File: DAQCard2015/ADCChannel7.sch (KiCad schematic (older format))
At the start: 50 parts, among them U10 LTC6403, U6 LTC6403, U7 AD9219, U8 LTC6403, U9 LTC6403

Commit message: Replaces single ample with 4-channel varients. Greatly reducing part count
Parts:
- removed C23, C33, C37, C38: .01uF, symbol C
- removed C24, C25, C29, C31, C32: .1uF, symbol C
- removed C26, C27, C28, C34, C35, C36, C39, C40, C41, C42, C43, C44: C, symbol C
- removed C30: 2.2uF, symbol CP
- removed R25, R32, R37, R38: Rt, symbol R
- removed R26, R27, R33, R34: Ri, symbol R
- removed R29, R30, R35, R36, R46: Rf, symbol R
- removed R31: 10k, symbol R
- removed R47: 2.7k, symbol R
- removed R48: 1k, symbol R
- removed U10, U6, U8, U9: LTC6403, symbol LTC6403
- removed U7: AD9219, symbol AD9219
- added C52, C53, C54: C, symbol C
- added C55: .01uF, symbol C
- added C56, C57, C58, C60, C61: .1uF, symbol C
- added C59: 2.2uF, symbol CP
- added RP16: R_PACK8, symbol R_PACK8
- added RP17, RP18: Rf, symbol R_PACK4
- added U12: THS4524IDBTR, symbol THS4524IDBTR
- added U13: AD9219, symbol AD9219
- R39, R40, R41, R42: value Ri -> Rt
- R43: value Rf -> 2.7k
- R44: value Rf -> 1k
- R45: value Rf -> 10k
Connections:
- net labels added: 3V3ana, VOCM
- net labels removed: 18ana, 3V3, Vocm
- wire segments 178 -> 192
- no-connect marks 12 -> 4
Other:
- note removed: "100R Termination \nis common for all ADCs."

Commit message: Finishes initial version of schematic(mostly). And adds a whole bunch of new footprints!
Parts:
- removed C53: C, symbol C
- removed C56, C57, C58, C60, C61: .1uF, symbol C
- removed C59: 2.2uF, symbol CP
- added C47: 10uF, extras:SMD_Cap_3mmDia, symbol CP
- added C48, C50, C51: .1uF, Capacitors_SMD:C_0603, symbol C
- added C49: .01uF, Capacitors_SMD:C_0603, symbol C
- added C53: 2.2uF, extras:SMD_Cap_3mmDia, symbol CP
- C52, C54: value C -> .1uF; footprint (none) -> Capacitors_SMD:C_0603
- C55: value .01uF -> .1uF; footprint (none) -> Capacitors_SMD:C_0603
- R39, R40, R41, R42, R43, R44, R45: footprint (none) -> Resistors_SMD:R_0603
- RP16: footprint (none) -> extras:R8_MNR18
- RP17, RP18: footprint (none) -> extras:R4-MNR04
- U12: footprint (none) -> Housings_SSOP:TSSOP-38_4.4x9.7mm_Pitch0.5mm
- U13: footprint (none) -> SMD_Packages:QFN-48-1EP
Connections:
- net 3V3ana: now also C47.1, C48.1; no longer C52.1, C54.1
- net ADC_CLK+: now also C51.2
- net ADC_CLK-: now also C50.2
- net GNDana: now also C55.1, C47.2, C48.2, C49.2; no longer C54.2, C55.2
- net VOCM: now also C49.1; no longer C55.1
- net at U13.7 (CLK-): now also C50.1
- net at U13.44 (REFT): now also C52.1, C54.2, C53.1
- net at U13.43 (REFB): now also C54.1, C55.2, C53.2
- net at U13.8 (CLK+): now also C51.1
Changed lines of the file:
@@
 $Descr A4 11693 8268
 encoding utf-8
-Sheet 3 13
+Sheet 8 13
 Title ""
 Date ""
@@
 $Comp
 L AD9219 U13
-U 1 1 55CFF5B0
+U 1 1 55CB5759
 P 9050 3700
 F 0 "U13" H 8250 4650 60  0000 C CNN
 F 1 "AD9219" H 9050 3800 60  0000 C CNN
-F 2 "" H 8650 3700 60  0000 C CNN
+F 2 "SMD_Packages:QFN-48-1EP" H 8650 3700 60  0001 C CNN
 F 3 "" H 8650 3700 60  0000 C CNN
 	1    9050 3700
@@
 $Comp
 L R R43
-U 1 1 55CFF5F3
+U 1 1 55CB5784
 P 3350 6700
 F 0 "R43" V 3430 6700 50  0000 C CNN
 F 1 "2.7k" V 3350 6700 50  0000 C CNN
-F 2 "" V 3280 6700 30  0000 C CNN
+F 2 "Resistors_SMD:R_0603" V 3280 6700 30  0001 C CNN
 F 3 "" H 3350 6700 30  0000 C CNN
 	1    3350 6700
@@
 $Comp
 L R R44
-U 1 1 55CFF5DC
+U 1 1 55CFF5DE
 P 3350 7100
 F 0 "R44" V 3430 7100 50  0000 C CNN
 F 1 "1k" V 3350 7100 50  0000 C CNN
-F 2 "" V 3280 7100 30  0000 C CNN
+F 2 "Resistors_SMD:R_0603" V 3280 7100 30  0001 C CNN
 F 3 "" H 3350 7100 30  0000 C CNN
 	1    3350 7100
@@
 Must terminate with 100R!
 $Comp
-L C C52
-U 1 1 55CFF5CD
-P 2650 6900
-F 0 "C52" H 2675 7000 50  0000 L CNN
-F 1 "C" H 2675 6800 50  0000 L CNN
-F 2 "" H 2688 6750 30  0000 C CNN
-F 3 "" H 2650 6900 60  0000 C CNN
-	1    2650 6900
-	1    0    0    -1
-$EndComp
-$Comp
-L C C53
-U 1 1 55CFF5B4
-P 2850 6900
-F 0 "C53" H 2875 7000 50  0000 L CNN
-F 1 "C" H 2875 6800 50  0000 L CNN
-F 2 "" H 2888 6750 30  0000 C CNN
-F 3 "" H 2850 6900 60  0000 C CNN
-	1    2850 6900
-	1    0    0    -1
-$EndComp
-$Comp
-L C C54
-U 1 1 55C4E847
+L C C48
+U 1 1 55CB575D
 P 3050 6900
-F 0 "C54" H 3075 7000 50  0000 L CNN
-F 1 "C" H 3075 6800 50  0000 L CNN
-F 2 "" H 3088 6750 30  0000 C CNN
+F 0 "C48" H 3075 7000 50  0000 L CNN
+F 1 ".1uF" H 3050 6800 50  0000 L CNN
+F 2 "Capacitors_SMD:C_0603" H 3088 6750 30  0001 C CNN
 F 3 "" H 3050 6900 60  0000 C CNN
 	1    3050 6900
@@
 ADC_SCLK
 $Comp
-L C C56
-U 1 1 55C50F50
+L C C50
+U 1 1 55CB5766
 P 7550 3650
-F 0 "C56" H 7575 3750 50  0000 L CNN
+F 0 "C50" H 7575 3750 50  0000 L CNN
 F 1 ".1uF" H 7575 3550 50  0000 L CNN
-F 2 "" H 7588 3500 30  0000 C CNN
+F 2 "Capacitors_SMD:C_0603" H 7588 3500 30  0001 C CNN
 F 3 "" H 7550 3650 60  0000 C CNN
 	1    7550 3650
@@
 $EndComp
 $Comp
-L C C57
-U 1 1 55CFF5E6
+L C C51
+U 1 1 55CB5745
 P 7550 3950
-F 0 "C57" H 7575 4050 50  0000 L CNN
+F 0 "C51" H 7575 4050 50  0000 L CNN
 F 1 ".1uF" H 7575 3850 50  0000 L CNN
-F 2 "" H 7588 3800 30  0000 C CNN
+F 2 "Capacitors_SMD:C_0603" H 7588 3800 30  0001 C CNN
 F 3 "" H 7550 3950 60  0000 C CNN
 	1    7550 3950
@@
 DCO+
 $Comp
-L C C61
-U 1 1 55CFF5FC
+L C C55
+U 1 1 55CB578C
 P 9300 1750
-F 0 "C61" H 9325 1850 50  0000 L CNN
+F 0 "C55" H 9325 1850 50  0000 L CNN
 F 1 ".1uF" H 9325 1650 50  0000 L CNN
-F 2 "" H 9338 1600 30  0000 C CNN
+F 2 "Capacitors_SMD:C_0603" H 9338 1600 30  0001 C CNN
 F 3 "" H 9300 1750 60  0000 C CNN
 	1    9300 1750
@@
 $EndComp
 $Comp
-L C C58
-U 1 1 55C98FC0
+L C C52
+U 1 1 55CB576C
 P 8600 1750
-F 0 "C58" H 8625 1850 50  0000 L CNN
+F 0 "C52" H 8625 1850 50  0000 L CNN
 F 1 ".1uF" H 8625 1650 50  0000 L CNN
-F 2 "" H 8638 1600 30  0000 C CNN
+F 2 "Capacitors_SMD:C_0603" H 8638 1600 30  0001 C CNN
 F 3 "" H 8600 1750 60  0000 C CNN
 	1    8600 1750
@@
 $EndComp
 $Comp
-L C C60
-U 1 1 55CFF5D7
+L C C54
+U 1 1 55CB5770
 P 8950 1650
-F 0 "C60" H 8975 1750 50  0000 L CNN
+F 0 "C54" H 8975 1750 50  0000 L CNN
 F 1 ".1uF" H 8975 1550 50  0000 L CNN
-F 2 "" H 8988 1500 30  0000 C CNN
+F 2 "Capacitors_SMD:C_0603" H 8988 1500 30  0001 C CNN
 F 3 "" H 8950 1650 60  0000 C CNN
 	1    8950 1650
@@
 GNDana
 $Comp
-L CP C59
-U 1 1 55CE4167
+L CP C53
+U 1 1 55CFF600
 P 8950 1450
-F 0 "C59" H 8975 1550 50  0000 L CNN
+F 0 "C53" H 8975 1550 50  0000 L CNN
 F 1 "2.2uF" H 8975 1350 50  0000 L CNN
-F 2 "" H 8988 1300 30  0000 C CNN
+F 2 "extras:SMD_Cap_3mmDia" H 8988 1300 30  0001 C CNN
 F 3 "" H 8950 1450 60  0000 C CNN
 	1    8950 1450
@@
 $Comp
 L R R45
-U 1 1 55CFF5EC
+U 1 1 55CB577E
 P 9900 1950
 F 0 "R45" V 9980 1950 50  0000 C CNN
 F 1 "10k" V 9900 1950 50  0000 C CNN
-F 2 "" V 9830 1950 30  0000 C CNN
+F 2 "Resistors_SMD:R_0603" V 9830 1950 30  0001 C CNN
 F 3 "" H 9900 1950 30  0000 C CNN
 	1    9900 1950
@@
 $Comp
 L THS4524IDBTR U12
-U 1 1 55CFF60B
+U 1 1 55CB579F
 P 4400 3700
 F 0 "U12" H 4700 2750 60  0000 C CNN
 F 1 "THS4524IDBTR" H 4400 4850 60  0000 C CNN
-F 2 "" H 4600 3800 60  0000 C CNN
+F 2 "Housings_SSOP:TSSOP-38_4.4x9.7mm_Pitch0.5mm" H 4600 3800 60  0001 C CNN
 F 3 "" H 4600 3800 60  0000 C CNN
 	1    4400 3700
@@
 $EndComp
 $Comp
-L C C55
-U 1 1 55CFF613
+L C C49
+U 1 1 55CB57A0
 P 3600 7100
-F 0 "C55" H 3625 7200 50  0000 L CNN
+F 0 "C49" H 3625 7200 50  0000 L CNN
 F 1 ".01uF" H 3625 7000 50  0000 L CNN
-F 2 "" H 3638 6950 30  0000 C CNN
+F 2 "Capacitors_SMD:C_0603" H 3638 6950 30  0001 C CNN
 F 3 "" H 3600 7100 60  0000 C CNN
 	1    3600 7100
@@
 Connection ~ 3600 6900
 Wire Wire Line
-	2650 6500 3750 6500
-Wire Wire Line
 	3050 6500 3050 6750
 Connection ~ 3350 6500
@@
 Connection ~ 3050 6500
 Wire Wire Line
-	2650 6500 2650 6750
-Connection ~ 2850 6500
-Wire Wire Line
-	2650 7300 3750 7300
-Wire Wire Line
 	3050 7300 3050 7050
 Wire Wire Line
 	2850 7300 2850 7050
 Connection ~ 3050 7300
-Wire Wire Line
-	2650 7300 2650 7050
-Connection ~ 2850 7300
 Wire Wire Line
 	3600 7300 3600 7250
@@
 $Comp
 L R R42
-U 1 1 55CFF617
+U 1 1 55CB57AD
 P 1850 4350
 F 0 "R42" V 1930 4350 50  0000 C CNN
 F 1 "Rt" V 1850 4350 50  0000 C CNN
-F 2 "" V 1780 4350 30  0000 C CNN
+F 2 "Resistors_SMD:R_0603" V 1780 4350 30  0001 C CNN
 F 3 "" H 1850 4350 30  0000 C CNN
 	1    1850 4350
@@
 $Comp
 L R R41
-U 1 1 55CF39BD
+U 1 1 55CB57B0
 P 1850 3850
 F 0 "R41" V 1930 3850 50  0000 C CNN
 F 1 "Rt" V 1850 3850 50  0000 C CNN
-F 2 "" V 1780 3850 30  0000 C CNN
+F 2 "Resistors_SMD:R_0603" V 1780 3850 30  0001 C CNN
 F 3 "" H 1850 3850 30  0000 C CNN
 	1    1850 3850
@@
 $Comp
 L R R40
-U 1 1 55CFF627
+U 1 1 55CB57B8
 P 1850 3350
 F 0 "R40" V 1930 3350 50  0000 C CNN
 F 1 "Rt" V 1850 3350 50  0000 C CNN
-F 2 "" V 1780 3350 30  0000 C CNN
+F 2 "Resistors_SMD:R_0603" V 1780 3350 30  0001 C CNN
 F 3 "" H 1850 3350 30  0000 C CNN
 	1    1850 3350
@@
 $Comp
 L R R39
-U 1 1 55CFF629
+U 1 1 55CB57C2
 P 1850 2850
 F 0 "R39" V 1930 2850 50  0000 C CNN
 F 1 "Rt" V 1850 2850 50  0000 C CNN
-F 2 "" V 1780 2850 30  0000 C CNN
+F 2 "Resistors_SMD:R_0603" V 1780 2850 30  0001 C CNN
 F 3 "" H 1850 2850 30  0000 C CNN
 	1    1850 2850
@@
 $Comp
 L R_PACK4 RP17
-U 1 1 55CFF630
+U 1 1 55CFF632
 P 4250 5150
 F 0 "RP17" H 4250 5600 50  0000 C CNN
 F 1 "Rf" H 4250 5100 50  0000 C CNN
-F 2 "" H 4250 5150 60  0000 C CNN
+F 2 "extras:R4-MNR04" H 4250 5150 60  0001 C CNN
 F 3 "" H 4250 5150 60  0000 C CNN
 	1    4250 5150
@@
 $Comp
 L R_PACK4 RP18
-U 1 1 55CFF639
+U 1 1 55CB574F
 P 4300 2450
 F 0 "RP18" H 4300 2900 50  0000 C CNN
 F 1 "Rf" H 4300 2400 50  0000 C CNN
-F 2 "" H 4300 2450 60  0000 C CNN
+F 2 "extras:R4-MNR04" H 4300 2450 60  0001 C CNN
 F 3 "" H 4300 2450 60  0000 C CNN
 	1    4300 2450
@@
 $Comp
 L R_PACK8 RP16
-U 1 1 55CFF63E
+U 1 1 55CB57CF
 P 2750 3600
 F 0 "RP16" H 2750 4050 50  0000 C CNN
 F 1 "R_PACK8" H 2750 3150 50  0000 C CNN
-F 2 "" H 2750 3600 60  0000 C CNN
+F 2 "extras:R8_MNR18" H 2750 3600 60  0001 C CNN
 F 3 "" H 2750 3600 60  0000 C CNN
 	1    2750 3600
@@
 Text GLabel 10150 1950 2    40   Input ~ 0
 GNDana
+Wire Wire Line
+	3750 6500 2850 6500
+Wire Wire Line
+	2850 7300 3750 7300
+$Comp
+L CP C47
+U 1 1 55CB5741
+P 2850 6900
+F 0 "C47" H 2875 7000 50  0000 L CNN
+F 1 "10uF" H 2850 6800 50  0000 L CNN
+F 2 "extras:SMD_Cap_3mmDia" H 2888 6750 30  0001 C CNN
+F 3 "" H 2850 6900 60  0000 C CNN
+	1    2850 6900
+	1    0    0    -1
+$EndComp
 $EndSCHEMATC

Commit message: Adds a more-or-less complete BOM to DAQ Card
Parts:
- C49: value .01uF -> 10000pF
- RP16: value R_PACK8 -> Ri
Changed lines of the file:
@@
 P 3600 7100
 F 0 "C49" H 3625 7200 50  0000 L CNN
-F 1 ".01uF" H 3625 7000 50  0000 L CNN
+F 1 "10000pF" H 3625 7000 50  0000 L CNN
 F 2 "Capacitors_SMD:C_0603" H 3638 6950 30  0001 C CNN
 F 3 "" H 3600 7100 60  0000 C CNN
@@
 P 2750 3600
 F 0 "RP16" H 2750 4050 50  0000 C CNN
-F 1 "R_PACK8" H 2750 3150 50  0000 C CNN
+F 1 "Ri" H 2750 3150 50  0000 C CNN
 F 2 "extras:R8_MNR18" H 2750 3600 60  0001 C CNN
 F 3 "" H 2750 3600 60  0000 C CNN

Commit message: Updates to DAQCard2015, especially to power systems
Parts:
- C47, C53: footprint extras:SMD_Cap_3mmDia -> Capacitors_SMD:C_0805
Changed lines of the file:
@@
 F 0 "C53" H 8975 1550 50  0000 L CNN
 F 1 "2.2uF" H 8975 1350 50  0000 L CNN
-F 2 "extras:SMD_Cap_3mmDia" H 8988 1300 30  0001 C CNN
+F 2 "Capacitors_SMD:C_0805" H 8988 1300 30  0001 C CNN
 F 3 "" H 8950 1450 60  0000 C CNN
 	1    8950 1450
@@
 F 0 "C47" H 2875 7000 50  0000 L CNN
 F 1 "10uF" H 2850 6800 50  0000 L CNN
-F 2 "extras:SMD_Cap_3mmDia" H 2888 6750 30  0001 C CNN
+F 2 "Capacitors_SMD:C_0805" H 2888 6750 30  0001 C CNN
 F 3 "" H 2850 6900 60  0000 C CNN
 	1    2850 6900

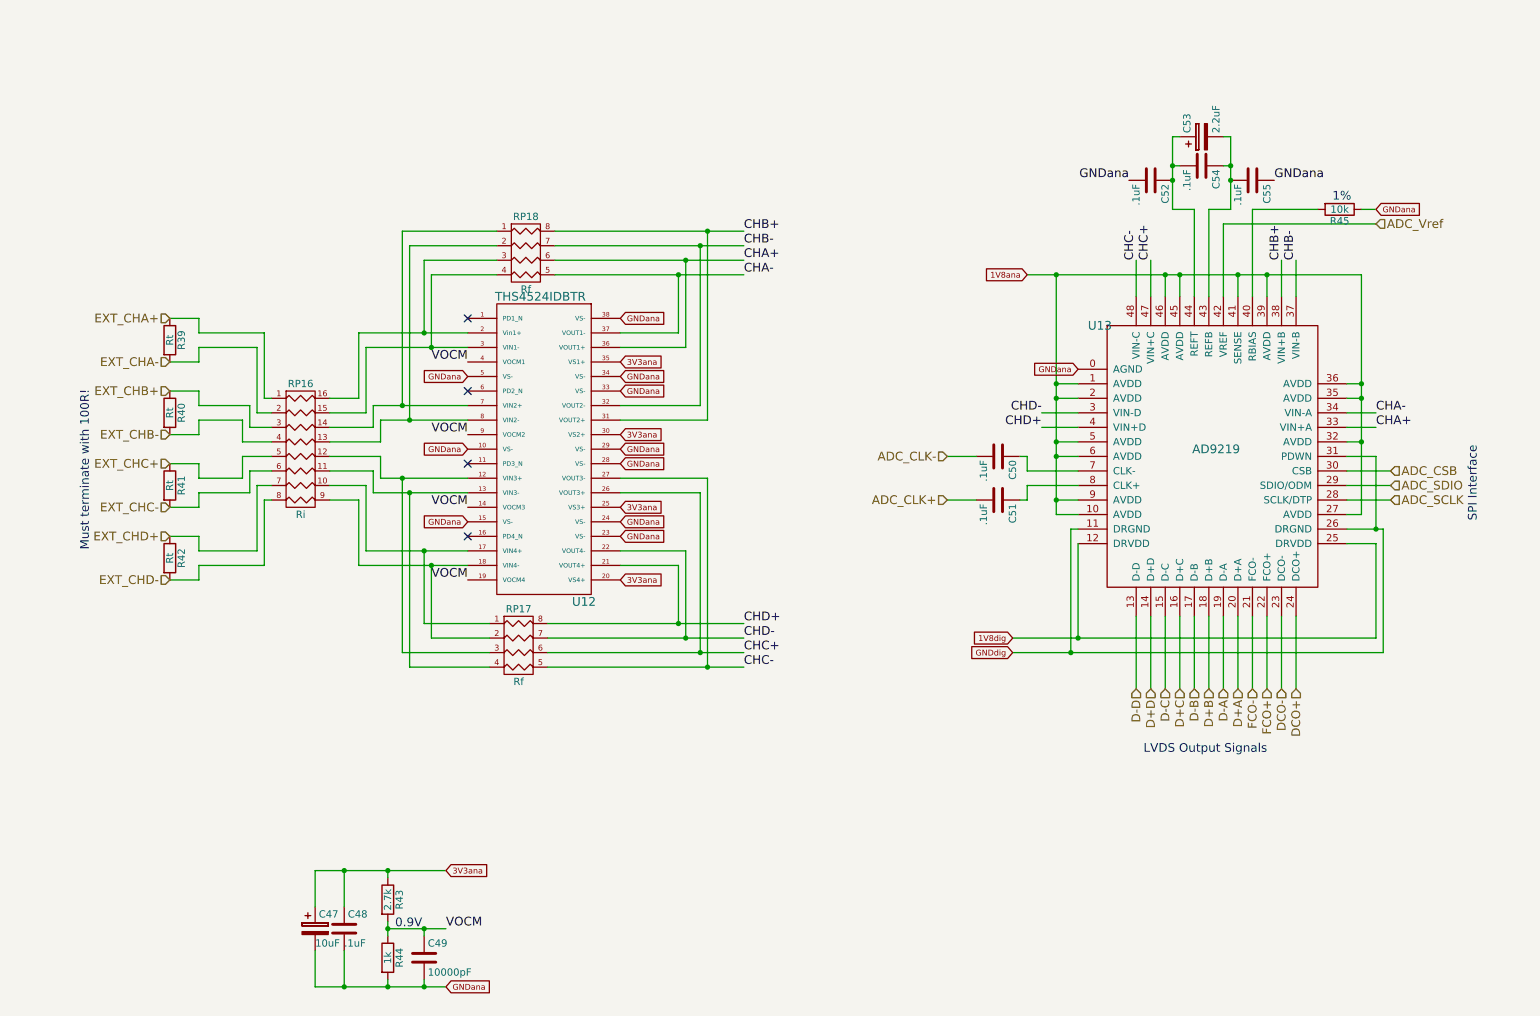
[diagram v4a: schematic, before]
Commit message: propogate previous changes to other channels and schematic
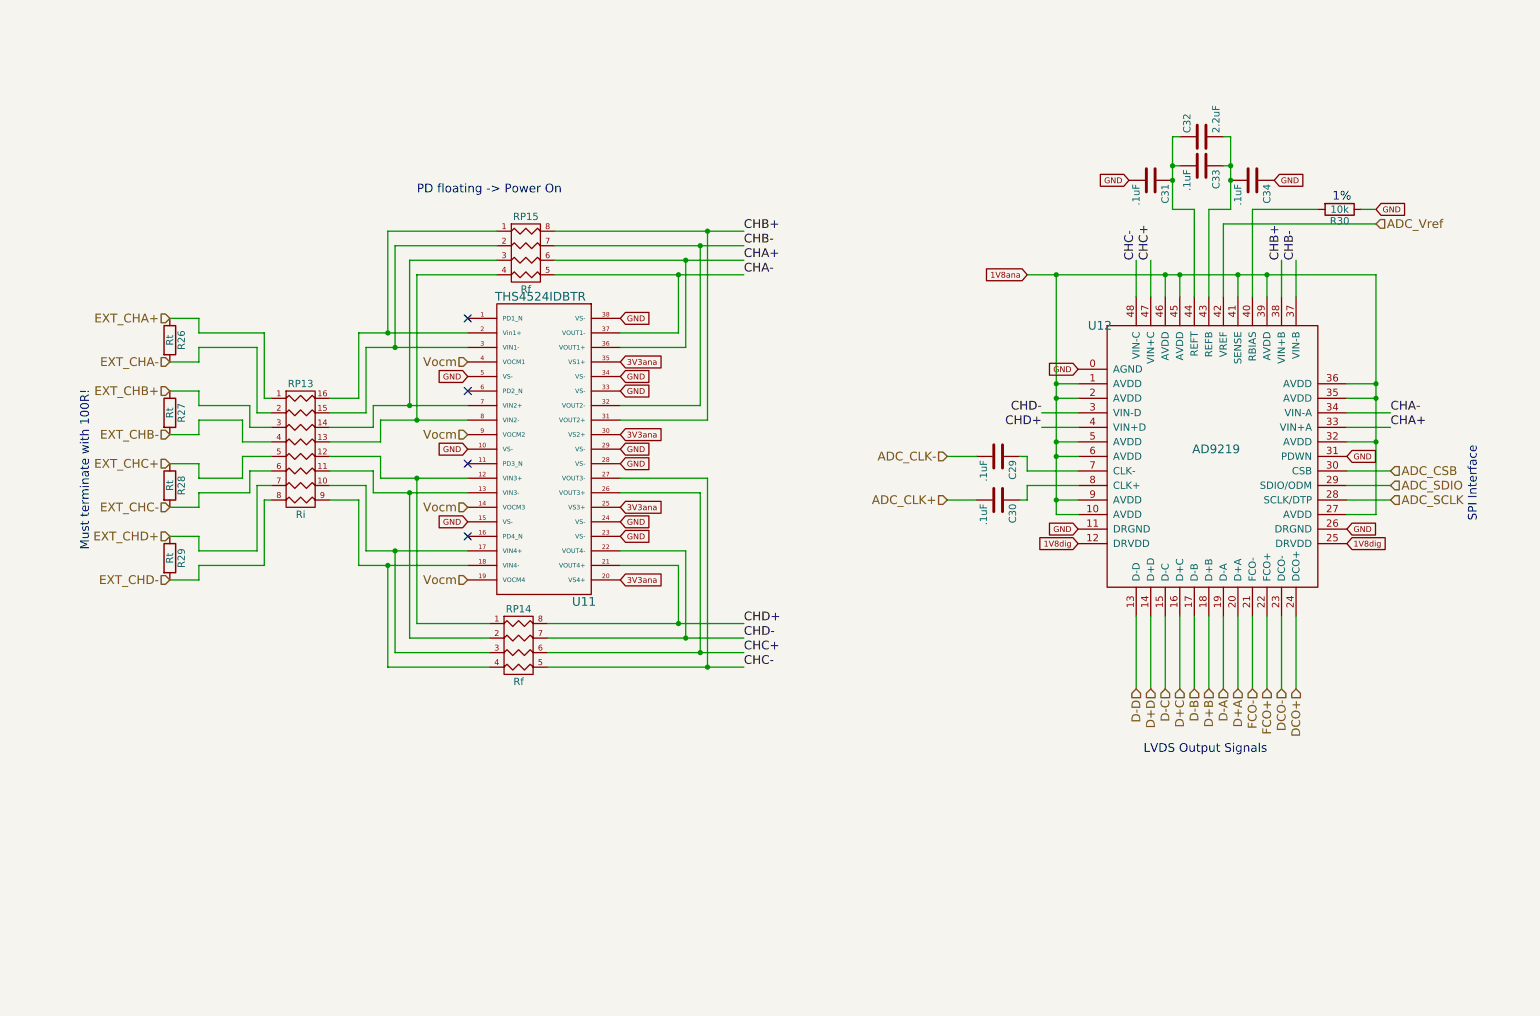
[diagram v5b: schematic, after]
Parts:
- removed C47: 10uF, Capacitors_SMD:C_0805, symbol CP
- removed C48, C50, C51, C52, C54, C55: .1uF, Capacitors_SMD:C_0603, symbol C
- removed C49: 10000pF, Capacitors_SMD:C_0603, symbol C
- removed C53: 2.2uF, Capacitors_SMD:C_0805, symbol CP
- removed R39, R40, R41, R42: Rt, Resistors_SMD:R_0603, symbol R
- removed R43: 2.7k, Resistors_SMD:R_0603, symbol R
- removed R44: 1k, Resistors_SMD:R_0603, symbol R
- removed R45: 10k, Resistors_SMD:R_0603, symbol R
- removed RP16: Ri, extras:R8_MNR18, symbol R_PACK8
- removed RP17, RP18: Rf, extras:R4-MNR04, symbol R_PACK4
- removed U12: THS4524IDBTR, Housings_SSOP:TSSOP-38_4.4x9.7mm_Pitch0.5mm, symbol THS4524IDBTR
- removed U13: AD9219, SMD_Packages:QFN-48-1EP, symbol AD9219
- added C29, C30, C31, C33, C34: .1uF, Capacitors_SMD:C_0603, symbol C
- added C32: 2.2uF, Capacitors_SMD:C_0805, symbol C
- added R26, R27, R28, R29: Rt, Resistors_SMD:R_0603, symbol R
- added R30: 10k, Resistors_SMD:R_0603, symbol R
- added RP13: Ri, extras:R8_MNR18, symbol R_PACK8
- added RP14, RP15: Rf, extras:R4-MNR04, symbol R_PACK4
- added U11: THS4524IDBTR, Housings_SSOP:TSSOP-38_4.4x9.7mm_Pitch0.5mm, symbol THS4524IDBTR
- added U12: AD9219, extras:QFN-48-1EP, symbol AD9219
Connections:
- net 1V8ana: now also U12.1 (AVDD), U12.10 (AVDD), U12.2 (AVDD), U12.27 (AVDD), U12.32 (AVDD), U12.35 (AVDD), U12.36 (AVDD), U12.39 (AVDD), U12.41 (SENSE), U12.45 (AVDD), U12.46 (AVDD), U12.5 (AVDD), U12.6 (AVDD), U12.9 (AVDD)
- net 1V8dig: now also U12.12 (DRVDD), U12.25 (DRVDD)
- net 3V3ana: now also U11.20 (VS4+), U11.25 (VS3+), U11.30 (VS2+), U11.35 (VS1+)
- net ADC_CLK+: now also C30.2
- net ADC_CLK-: now also C29.2
- net ADC_CSB: now also U12.30 (CSB)
- net ADC_SCLK: now also U12.28 (SCLK/DTP)
- net ADC_SDIO: now also U12.29 (SDIO/ODM)
- net ADC_Vref: now also U12.42 (VREF)
- net CHA+: now also RP15.6 (R3), U11.36 (VOUT1+), U12.33 (VIN+A)
- net CHA-: now also RP15.5 (R4), U11.37 (VOUT1-), U12.34 (VIN-A)
- net CHB+: now also RP15.8 (R1), U11.31 (VOUT2+), U12.38 (VIN+B)
- net CHB-: now also RP15.7 (R2), U11.32 (VOUT2-), U12.37 (VIN-B)
- net CHC+: now also RP14.6 (R3), U11.26 (VOUT3+), U12.47 (VIN+C)
- net CHC-: now also RP14.5 (R4), U11.27 (VOUT3-), U12.48 (VIN-C)
- net CHD+: now also RP14.8 (R1), U11.21 (VOUT4+), U12.4 (VIN+D)
- net CHD-: now also RP14.7 (R2), U11.22 (VOUT4-), U12.3 (VIN-D)
- net D+A: now also U12.20 (D+A)
- net D+B: now also U12.18 (D+B)
- net D+C: now also U12.16 (D+C)
- net D+D: now also U12.14 (D+D)
- net D-A: now also U12.19 (D-A)
- net D-B: now also U12.17 (D-B)
- net D-C: now also U12.15 (D-C)
- net D-D: now also U12.13 (D-D)
- net DCO+: now also U12.24 (DCO+)
- net DCO-: now also U12.23 (DCO-)
- net EXT_CHA+: now also R26.1, RP13.1 (P1)
- net EXT_CHA-: now also R26.2, RP13.2 (P2)
- net EXT_CHB+: now also R27.1, RP13.3 (P3)
- net EXT_CHB-: now also R27.2, RP13.4 (P4)
- net EXT_CHC+: now also R28.1, RP13.5 (P5)
- net EXT_CHC-: now also R28.2, RP13.6 (P6)
- net EXT_CHD+: now also R29.1, RP13.7 (P7)
- net EXT_CHD-: now also R29.2, RP13.8 (P8)
- net FCO+: now also U12.22 (FCO+)
- net FCO-: now also U12.21 (FCO-)
- new net: C32.2, C33.1, C34.2, U12.43 (REFB)
- new net: C31.1, C32.1, C33.2, U12.44 (REFT)
- new net: RP13.12 (R5), RP14.1 (P1), U11.12 (VIN3+)
- new net: RP13.11 (R6), RP14.2 (P2), U11.13 (VIN3-)
- new net: RP13.10 (R7), RP14.3 (P3), U11.17 (VIN4+)
- new net: RP13.9 (R8), RP14.4 (P4), U11.18 (VIN4-)
- new net: C30.1, U12.8 (CLK+)
- new net: RP13.16 (R1), RP15.1 (P1), U11.2 (Vin1+)
- new net: RP13.15 (R2), RP15.2 (P2), U11.3 (VIN1-)
- new net: RP13.14 (R3), RP15.3 (P3), U11.7 (VIN2+)
- new net: RP13.13 (R4), RP15.4 (P4), U11.8 (VIN2-)
- new net: R30.2, U12.40 (RBIAS)
- new net: C29.1, U12.7 (CLK-)
- new net GND: C31.2, C34.1, R30.1, U11.10 (VS-), U11.15 (VS-), U11.23 (VS-), U11.24 (VS-), U11.28 (VS-), U11.29 (VS-), U11.33 (VS-), U11.34 (VS-), U11.38 (VS-), U11.5 (VS-), U12.0 (AGND), U12.11 (DRGND), U12.26 (DRGND), U12.31 (PDWN)
- new net Vocm: U11.14 (VOCM3), U11.19 (VOCM4), U11.4 (VOCM1), U11.9 (VOCM2)
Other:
- note added: "PD floating -> Power On"
- note removed: "0.9V"

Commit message: Various updates to DAQ board focusing on power system
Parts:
- U11: footprint Housings_SSOP:TSSOP-38_4.4x9.7mm_Pitch0.5mm -> extras:TSSOP-38_4.4x9.7mm_Pitch0.5mm
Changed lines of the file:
@@
 F 0 "U11" H 4700 2750 60  0000 C CNN
 F 1 "THS4524IDBTR" H 4400 4850 60  0000 C CNN
-F 2 "Housings_SSOP:TSSOP-38_4.4x9.7mm_Pitch0.5mm" H 4600 3800 60  0001 C CNN
+F 2 "extras:TSSOP-38_4.4x9.7mm_Pitch0.5mm" H 4600 3800 60  0001 C CNN
 F 3 "" H 4600 3800 60  0000 C CNN
 	1    4400 3700
